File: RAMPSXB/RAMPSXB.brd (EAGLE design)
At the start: 129.5 x 73.5 mm, 95 parts, among them CN1 1X4-BIG, CN2 1X4-BIG, CN3 1X4-BIG, CN4 1X4-BIG, CN5 1X4-BIG, CN6 1X4-BIG, CN7 1X4-BIG, CN8 1X4-BIG, CN9 1X4-BIG, J1 1X2-3.5MM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

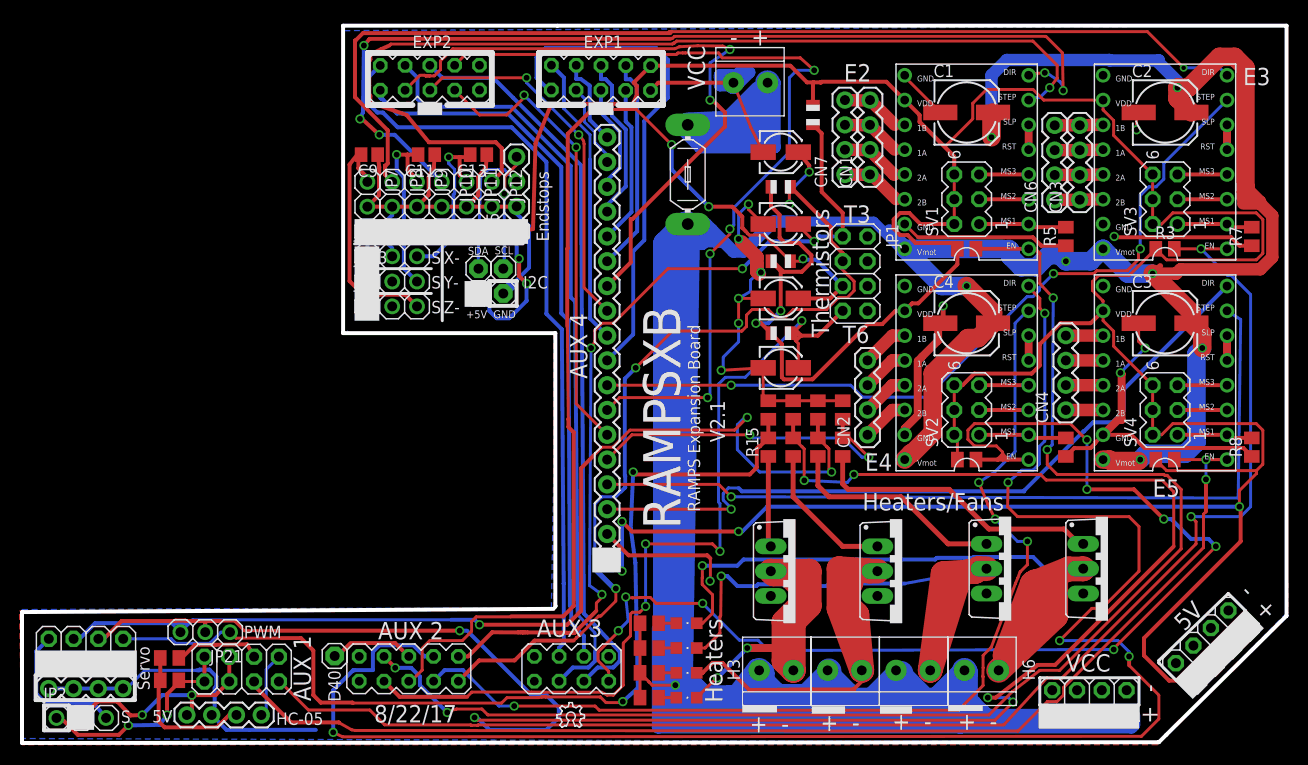
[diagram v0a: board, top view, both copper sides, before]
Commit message: Added Power Indicator and fixed a short.
Added Power indicator LED, and Fixed a major issue where +5V on the
arduino was connected to ground. Whoops.
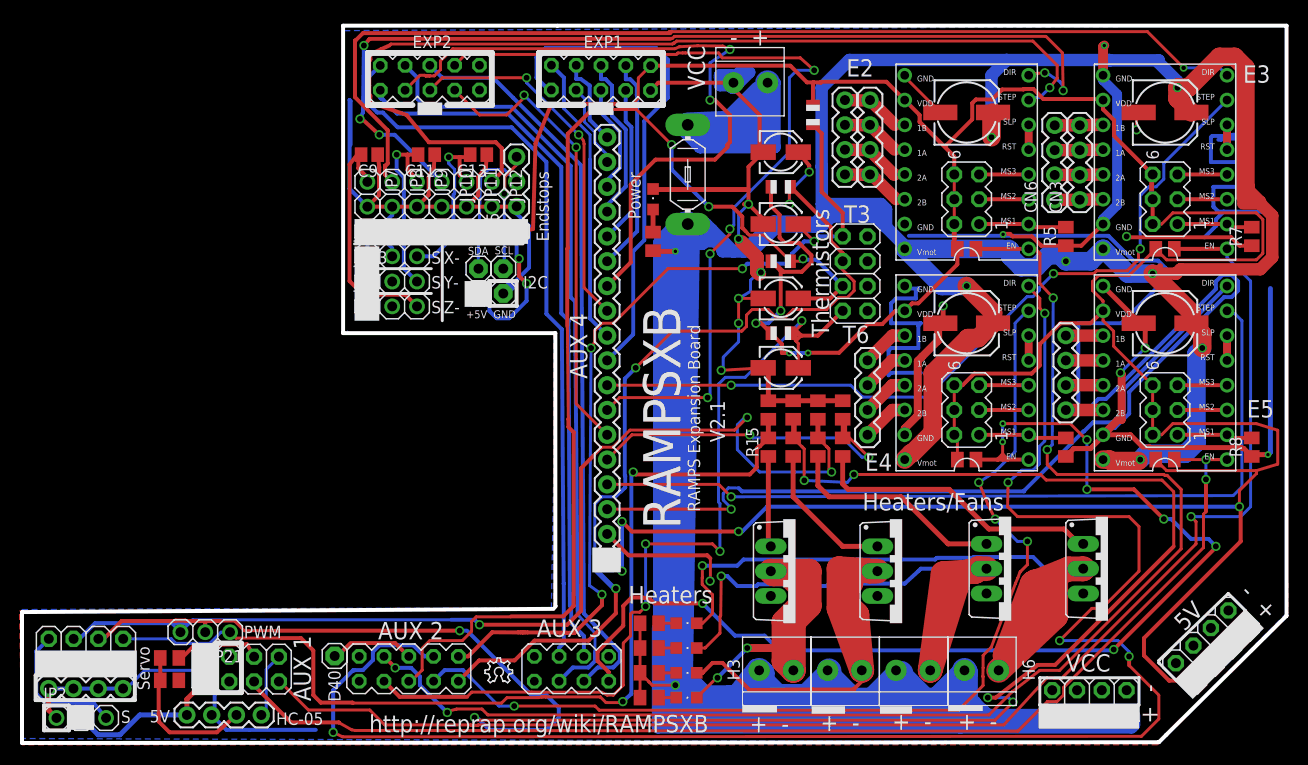
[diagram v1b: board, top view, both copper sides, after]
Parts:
- added LED5: (no value), adafruit:CHIPLED_0805
- added R27: 1.8k, adafruit:M0805
- moved LOGO1 8.67 mm to (15.3, 5.33)
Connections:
- new net N$2: LED5.A, R27.2
- net +12V: now also R27.1
- net 5V: now also JP5.1, JP5.2; no longer JP5.3, JP5.4
- net GND: now also JP2.1, JP5.3, JP5.4, LED5.C
- net GND1: no longer JP2.1, JP5.1, JP5.2
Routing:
- net GND: track 272.5 -> 495.5 mm, vias 12 -> 15
- net +12V: track 577.4 -> 641.2 mm, vias 8 -> 9
- net GND1: track 22.2 -> 0.00 mm, vias 2 -> 0
- net D49: track 124.0 -> 117.6 mm
- net D58: track 147.4 -> 153.2 mm, vias 2 -> 1
- net D31: track 67.4 -> 71.4 mm
- net 5V: track 22.7 -> 19.1 mm, vias 2 -> 0
- net N$2: track 0.00 -> 2.32 mm
- net D5: track 205.8 -> 207.9 mm
- net A12: track 99.2 -> 101.2 mm
- net D45: track 34.2 -> 36.2 mm
- net +5V: track 454.4 -> 455.7 mm, vias 8 -> 10
- net D42: track 174.8 -> 174.2 mm
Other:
- board text added: "Power"
- board text added: "http://reprap.org/wiki/RAMPSXB"
- board text removed: "8/22/17"

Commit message: Added Gerber Files. Slight Rewiring.
Added Gerber Files for production run. Fixed some clearance issues.
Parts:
- removed C13: 0.47uF, adafruit:C0805
- added C10: 0.47uF, adafruit:C0805
- moved C11 5.33 mm to (14.6, 59.4)
- renumbered F2 to F1
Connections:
- net D14: now also C10.2; no longer C11.2
- net D18: now also C11.2; no longer C13.2
- net GND: now also C10.1; no longer C13.1
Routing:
- net GND: track 495.5 -> 478.6 mm
- net +5V: track 455.7 -> 471.3 mm, vias 10 -> 9
- net D32: track 76.7 -> 88.6 mm
- net N$37: track 61.5 -> 65.7 mm
- net D49: track 117.6 -> 120.2 mm
- net N$38: track 83.1 -> 84.3 mm
- net D44: track 103.8 -> 104.8 mm
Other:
- board text added: "+5V Power"
- board text added: "0.47uF"
- board text added: "1.8k"
- board text added: "100k"
- board text added: "100uF"
- board text added: "10k"
- board text added: "10r"
- board text added: "10uF"
- board text added: "2.2k"
- board text added: "3.3k"
- board text added: "4.7k"
- board text added: "A10"
- board text added: "A11"
- board text added: "A12"
- board text added: "A5"
- board text added: "C1"
- board text added: "C10"
- board text added: "C11"
- board text added: "C2"
- board text added: "C3"
- board text added: "C4"
- board text added: "C5"
- board text added: "C6"
- board text added: "C7"
- board text added: "C8"
- board text added: "C9"
- board text added: "D0"
- board text added: "D1"
- board text added: "D11"
- board text added: "D14"
- board text added: "D15"
- board text added: "D16"
- board text added: "D17"
- board text added: "D18"
- board text added: "D19"
- board text added: "D2"
- board text added: "D20"
- board text added: "D21"
- board text added: "D23"
- board text added: "D25"
- board text added: "D27"
- board text added: "D29"
- board text added: "D3"
- board text added: "D31"
- board text added: "D32"
- board text added: "D33"
- board text added: "D35"
- board text added: "D37"
- board text added: "D39"
- board text added: "D4"
- board text added: "D41"
- board text added: "D43"
- board text added: "D44"
- board text added: "D45"
- board text added: "D47"
- board text added: "D49"
- board text added: "D5"
- board text added: "D50"
- board text added: "D51"
- board text added: "D52"
- board text added: "D53"
- board text added: "D57"
- board text added: "D58"
- board text added: "D6"
- board text added: "D63"
- board text added: "DIR"
- board text added: "Disc"
- board text added: "EN"
- board text added: "F1"
- board text added: "LED1"
- board text added: "LED2"
- board text added: "LED3"
- board text added: "LED4"
- board text added: "LED5"
- board text added: "MOSFET 3"
- board text added: "MOSFET 4"
- board text added: "MOSFET 5"
- board text added: "MOSFET 6"
- board text added: "NC"
- board text added: "Pin"
- board text added: "Q1"
- board text added: "Q2"
- board text added: "Q3"
- board text added: "Q4"
- board text added: "R1"
- board text added: "R10"
- board text added: "R11"
- board text added: "R12"
- board text added: "R13"
- board text added: "R14"
- board text added: "R15"
- board text added: "R16"
- board text added: "R17"
- board text added: "R18"
- board text added: "R19"
- board text added: "R2"
- board text added: "R20"
- board text added: "R21"
- board text added: "R22"
- board text added: "R23"
- board text added: "R24"
- board text added: "R25"
- board text added: "R26"
- board text added: "R27"
- board text added: "R3"
- board text added: "R4"
- board text added: "R5"
- board text added: "R6"
- board text added: "R7"
- board text added: "R8"
- board text added: "R9"
- board text added: "RX"
- board text added: "STEP"
- board text added: "TX"
- board text added: "Thermistor 3"
- board text added: "Thermistor 4"
- board text added: "Thermistor 5"
- board text added: "Thermistor 6"
- board text added: "VCC Power"

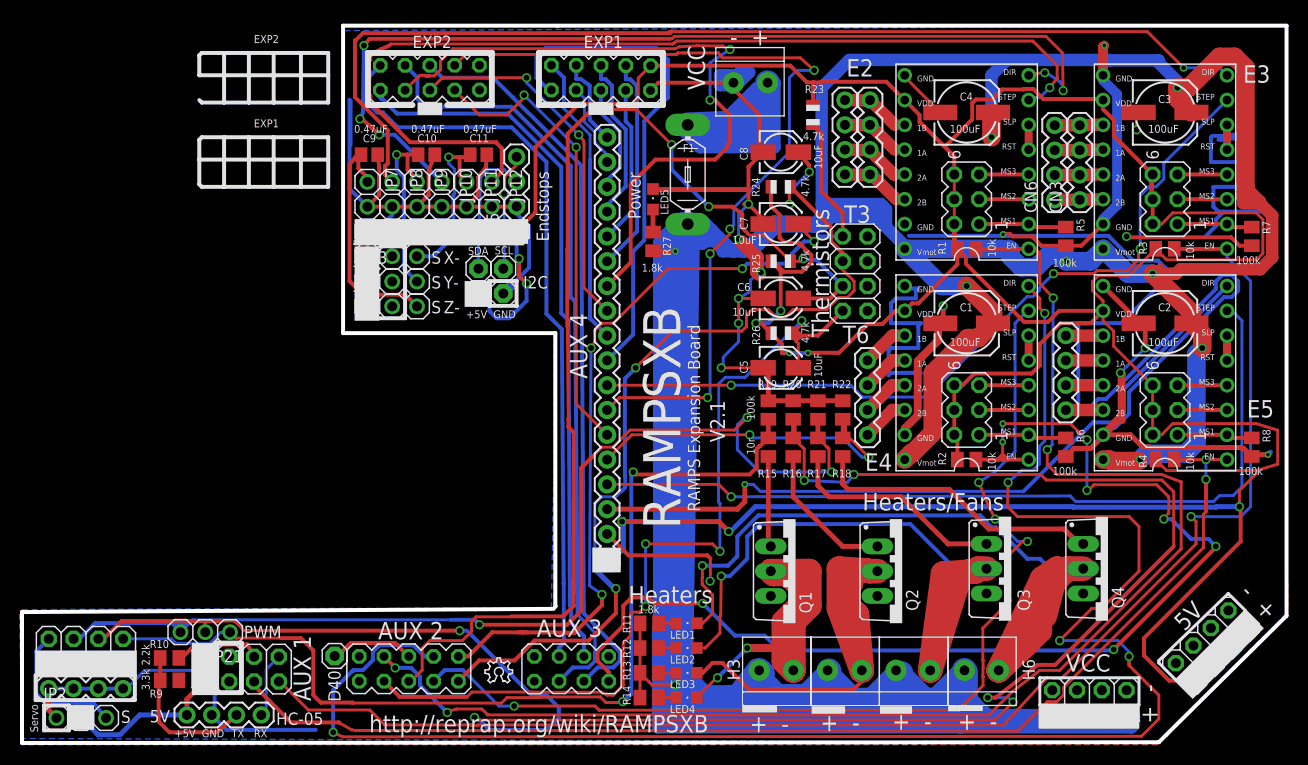
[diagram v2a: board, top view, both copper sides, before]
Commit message: Swapped pins 49 and 43. Documentation for the Smart Controller was incorrect.
Almost everything works, but the SD card for some reason opens, but I
cant read anything. Still working on that.
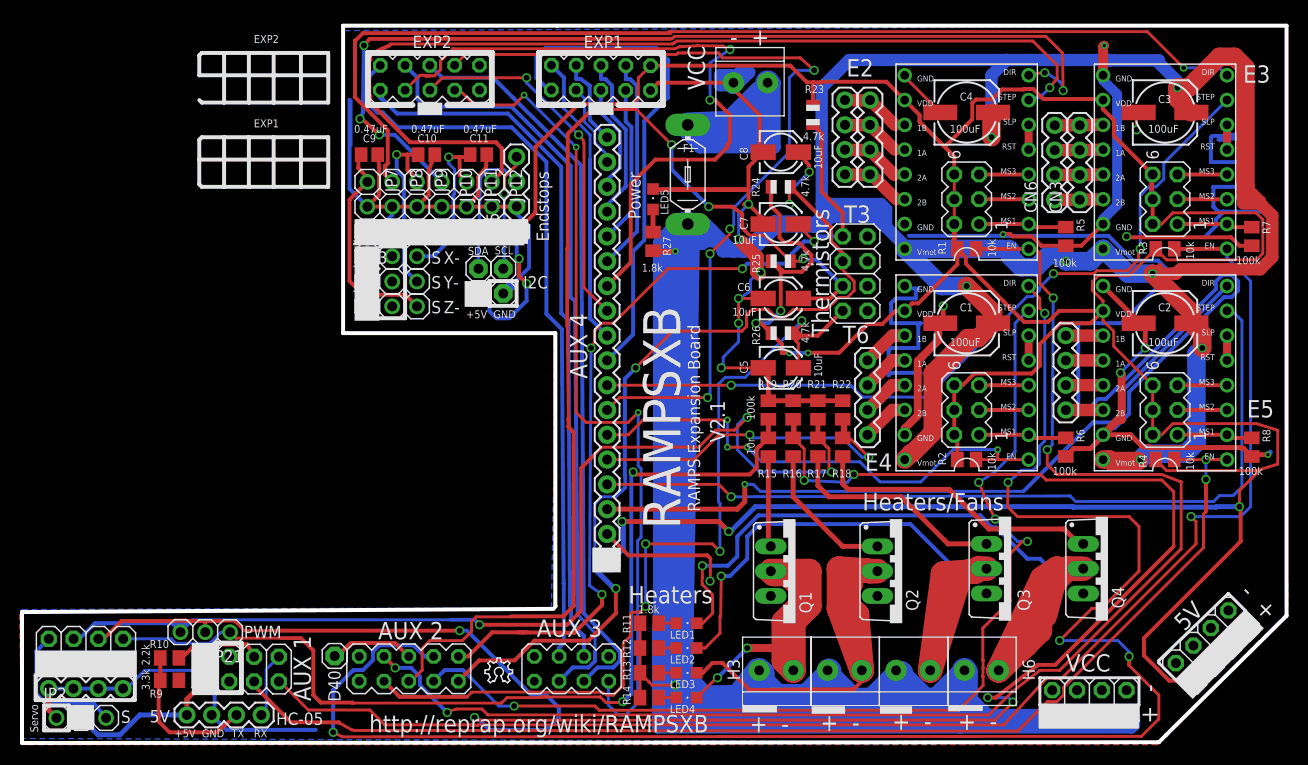
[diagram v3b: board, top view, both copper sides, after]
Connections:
- net +5V: now also U$3.1
- net D43: now also R2.2, U$2.EN; no longer EXP2.7
- net D49: now also EXP2.7; no longer R2.2, U$2.EN
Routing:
- net D49: track 120.2 -> 86.5 mm, vias 8 -> 3
- net D43: track 47.5 -> 52.7 mm, vias 2 -> 4
- net D3: track 26.2 -> 23.3 mm
